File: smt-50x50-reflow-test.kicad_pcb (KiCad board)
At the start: 4 copper layers, 50 x 50 mm, 96 parts, among them J1 Conn_01x04_Pin, J2 Conn_01x02, J4 USB_C_Receptacle_USB2.0_14P, J8 Conn_01x04_Pin, J9 Conn_01x03_Pin, SW1 SW_Push, SW2 SW_Push, U1 ESP32-C6, U14 TMP117AIDRV, U15 BMP581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

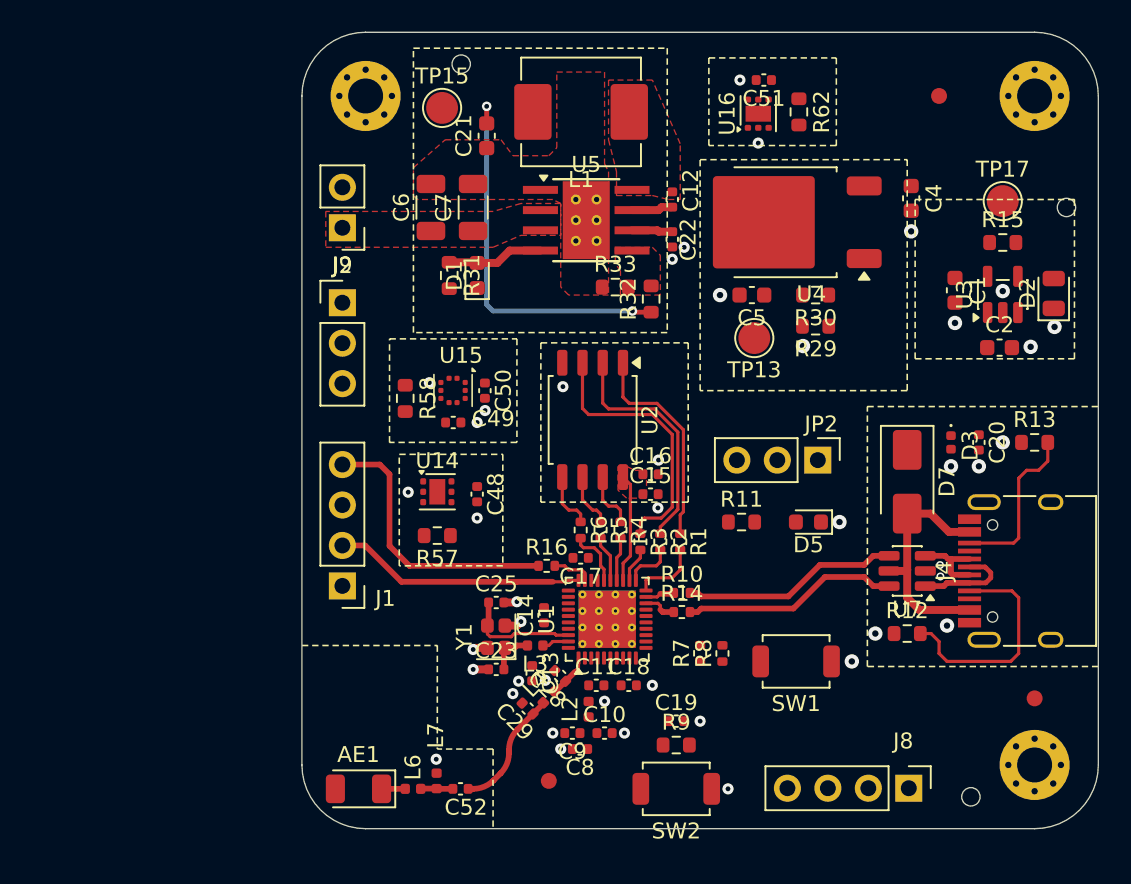
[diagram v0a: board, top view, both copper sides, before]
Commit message: pcb: add 3v3 routing
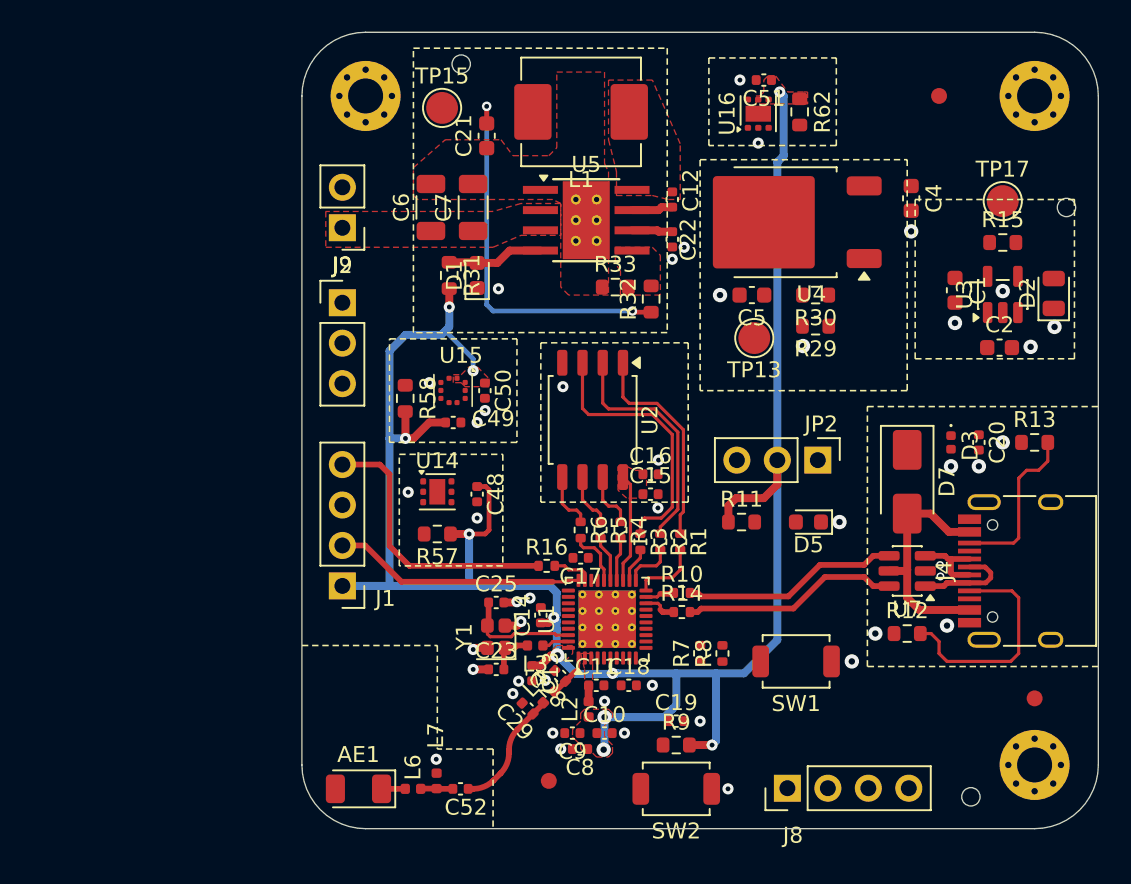
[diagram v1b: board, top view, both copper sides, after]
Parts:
- moved J8 7.62 mm to (165.5, 122.5), turned to 90 degrees
- moved C14 0.20 mm to (150.0, 111.6)
- moved R57 0.10 mm to (143.5, 106.5)
- moved R62 0.05 mm to (166.2, 80.0)
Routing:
- net +3V3: track 0.00 -> 131.3 mm, vias 0 -> 11
- net Net-(C11-Pad1): track 0.00 -> 1.02 mm
- net GND: vias 43 -> 45
- added copper zone on F.Cu, net +3V3
- added copper zone on F.Cu, net Net-(C11-Pad1)

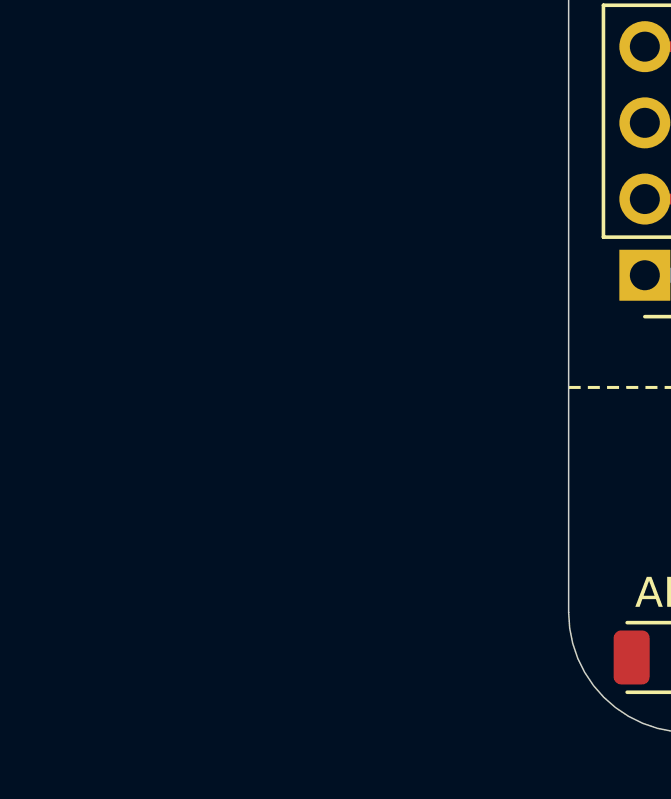
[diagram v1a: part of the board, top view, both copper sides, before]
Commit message: pcb: import smol area from schem
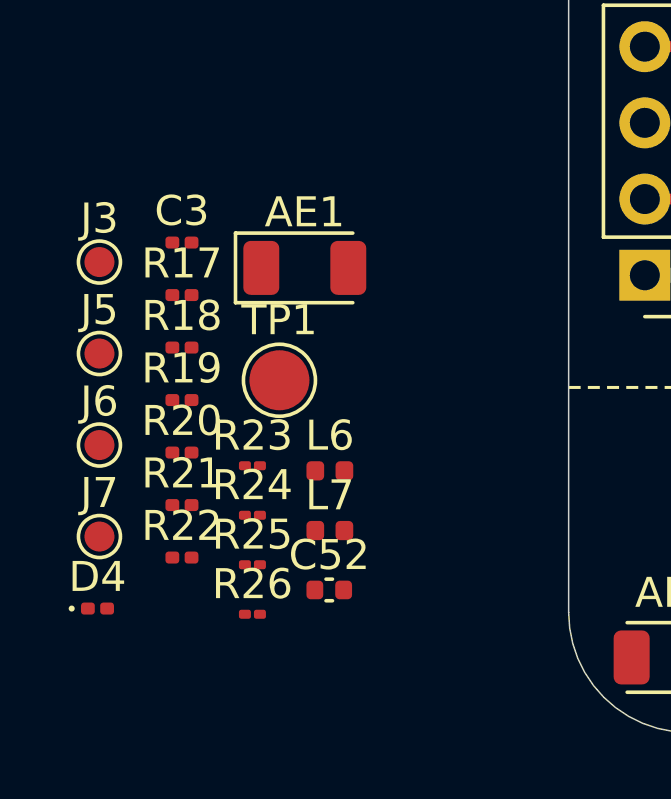
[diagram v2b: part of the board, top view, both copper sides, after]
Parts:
- added AE1: Antenna, RF_Antenna:Johanson_2450AT18x100, F.Cu at (126.2, 109.5)
- added C3: 2k2, Capacitor_SMD:C_0201_0603Metric, F.Cu at (122.1, 108.7)
- added C52: 1p, Capacitor_SMD:C_0402_1005Metric, F.Cu at (127.0, 120.2)
- added D4: ORANGE, LED_SMD:LED_0201_0603Metric, F.Cu at (119.3, 120.9)
- added J3: Conn_01x01, TestPoint:TestPoint_Pad_D1.0mm, F.Cu at (119.4, 109.3)
- added J5: Conn_01x01, TestPoint:TestPoint_Pad_D1.0mm, F.Cu at (119.4, 112.4)
- added J6: Conn_01x01, TestPoint:TestPoint_Pad_D1.0mm, F.Cu at (119.4, 115.4)
- added J7: Conn_01x01, TestPoint:TestPoint_Pad_D1.0mm, F.Cu at (119.4, 118.5)
- added L6: 3n9, Inductor_SMD:L_0402_1005Metric, F.Cu at (127.0, 116.3)
- added L7: 2n7, Inductor_SMD:L_0402_1005Metric, F.Cu at (127.0, 118.3)
- added R17: 5k1, Resistor_SMD:R_0201_0603Metric, F.Cu at (122.1, 110.4)
- added R18: 5k1, Resistor_SMD:R_0201_0603Metric, F.Cu at (122.1, 112.2)
- added R19: 10k, Resistor_SMD:R_0201_0603Metric, F.Cu at (122.1, 113.9)
- added R20: 24k, Resistor_SMD:R_0201_0603Metric, F.Cu at (122.1, 115.7)
- added R21: 70, Resistor_SMD:R_0201_0603Metric, F.Cu at (122.1, 117.4)
- added R22: 39k, Resistor_SMD:R_0201_0603Metric, F.Cu at (122.1, 119.2)
- added R23: 20k, Resistor_SMD:R_01005_0402Metric, F.Cu at (124.5, 116.1)
- added R24: 750, Resistor_SMD:R_01005_0402Metric, F.Cu at (124.5, 117.8)
- added R25: 1k33, Resistor_SMD:R_01005_0402Metric, F.Cu at (124.5, 119.4)
- added R26: 4k3, Resistor_SMD:R_01005_0402Metric, F.Cu at (124.5, 121.1)
- added TP1: TestPoint, TestPoint:TestPoint_Pad_D2.0mm, F.Cu at (125.4, 113.3)
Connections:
- U1 pad 31: unconnected-(U1-GPIO18/SDIO_CMD/FSPICS2-Pad31) -> Net-(U1-GPIO18/SDIO_CMD/FSPICS2)
- U1 pad 32: unconnected-(U1-GPIO19/SDIO_CLK/FSPICS3-Pad32) -> Net-(U1-GPIO19/SDIO_CLK/FSPICS3)
- U1 pad 34: unconnected-(U1-GPIO21/SDIO_DATA1/FSPICS5-Pad34) -> /BMP_INT1
- U1 pad 35: unconnected-(U1-GPIO22/SDIO_DATA2-Pad35) -> /TMP117_ALERT
- U1 pad 36: unconnected-(U1-GPIO23/SDIO_DATA3-Pad36) -> /TMP117_ALERT2
- U1 pad 6: /XTAL_32K_P -> unconnected-(U1-GPIO0/XTAL_32K_P/ADC1_CH0-Pad6)
- U1 pad 7: /XTAL_32K_N -> unconnected-(U1-GPIO1/XTAL_32K_N/ADC1_CH1-Pad7)

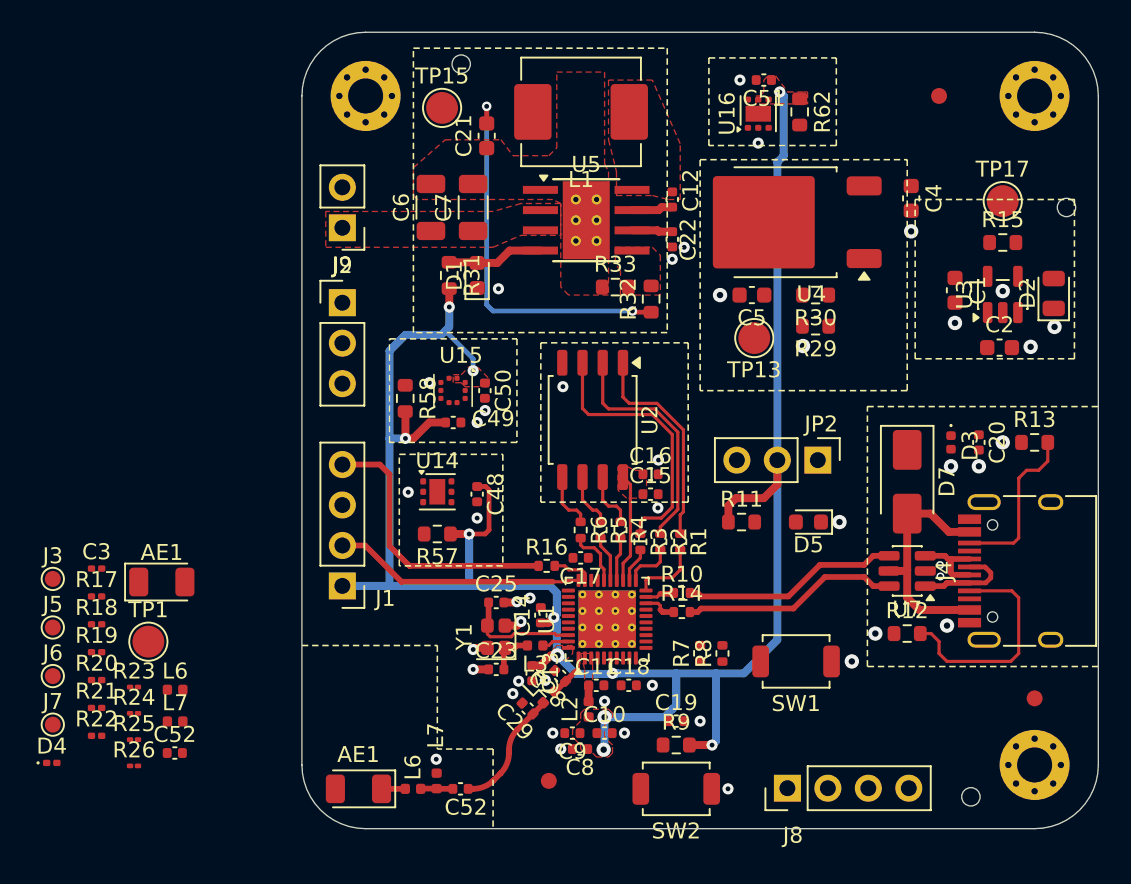
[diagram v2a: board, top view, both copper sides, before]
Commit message: pcb: add smol area layout
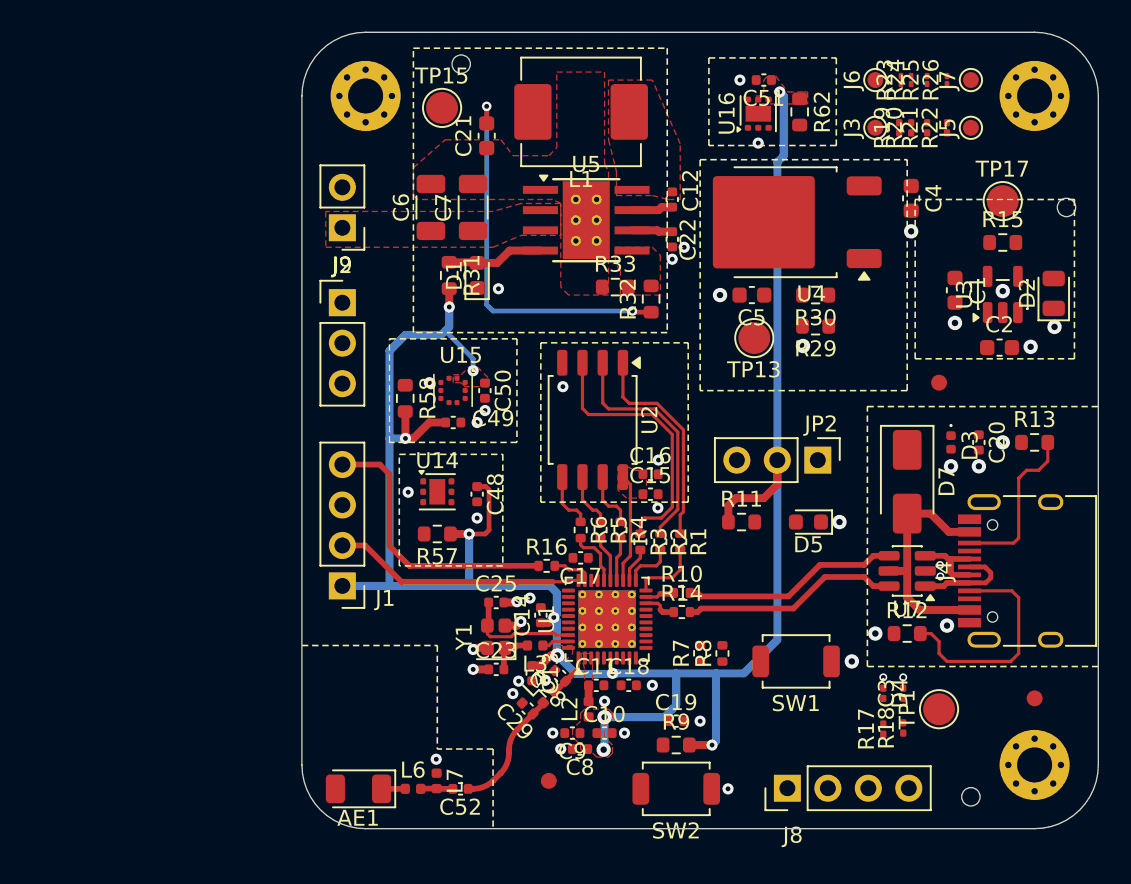
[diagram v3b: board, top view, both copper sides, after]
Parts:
- removed the AE1 at (138.6, 122.5)
- removed the C52 at (145.0, 122.5)
- removed the L6 at (142.0, 122.5)
- removed the L7 at (143.5, 122.0)
- moved J7 70.4 mm to (177.0, 78.0), turned to 90 degrees
- moved R26 66.8 mm to (175.5, 78.0), turned to 90 degrees
- moved R22 65.6 mm to (175.5, 81.0), turned to 90 degrees
- moved J5 65.6 mm to (177.0, 81.0), turned to 90 degrees
- moved R25 64.8 mm to (174.2, 78.0), turned to 90 degrees
- moved J6 63.8 mm to (171.0, 78.0), turned to 90 degrees
- moved R21 63.6 mm to (174.2, 81.0), turned to 90 degrees
- moved R24 62.9 mm to (173.2, 78.0), turned to 90 degrees
- moved R20 61.8 mm to (173.2, 81.0), turned to 90 degrees
- moved R23 61.4 mm to (172.6, 78.0), turned to 90 degrees
- moved R19 60.2 mm to (172.5, 81.0), turned to 90 degrees
- moved J3 58.9 mm to (171.0, 81.0), turned to 90 degrees
- moved D4 52.4 mm to (171.5, 116.5), turned to -90 degrees
- moved C3 51.2 mm to (172.8, 116.5), turned to 90 degrees
- moved R18 51.1 mm to (172.8, 118.7), turned to 90 degrees
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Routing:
- net GND: vias 45 -> 47

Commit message: pcb: add smol area routing
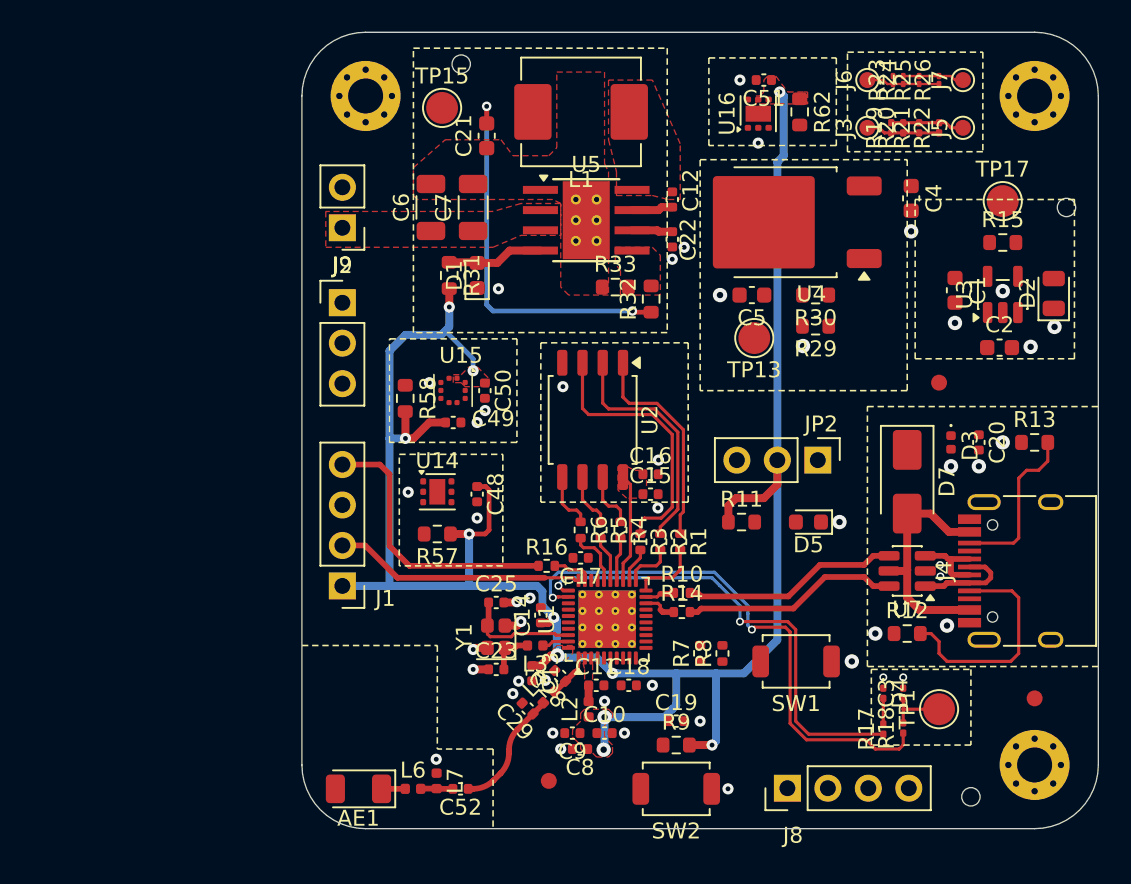
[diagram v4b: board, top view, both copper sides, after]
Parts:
- moved J3 0.50 mm to (170.5, 81.0)
- moved J5 0.50 mm to (176.5, 81.0)
- moved J6 0.50 mm to (170.5, 78.0)
- moved J7 0.50 mm to (176.5, 78.0)
- moved R19 0.50 mm to (172.0, 81.0)
- moved R20 0.50 mm to (172.8, 81.0)
- moved R21 0.50 mm to (173.8, 81.0)
- moved R22 0.50 mm to (175.0, 81.0)
- moved R23 0.50 mm to (172.1, 78.0)
- moved R24 0.50 mm to (172.8, 78.0)
- moved R25 0.50 mm to (173.8, 78.0)
- moved R26 0.50 mm to (175.0, 78.0)
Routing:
- net Net-(U1-GPIO19/SDIO_CLK/FSPICS3): track 0.00 -> 34.2 mm, vias 0 -> 2
- net Net-(U1-GPIO18/SDIO_CMD/FSPICS2): track 0.00 -> 29.4 mm, vias 0 -> 2
- net Net-(J5-Pin_1): track 0.00 -> 4.63 mm
- net Net-(J3-Pin_1): track 0.00 -> 4.63 mm
- net Net-(J6-Pin_1): track 0.00 -> 4.60 mm
- net Net-(J7-Pin_1): track 0.00 -> 4.49 mm
- net Net-(C3-Pad1): track 0.00 -> 3.79 mm
- net Net-(D4-A): track 0.00 -> 1.61 mm
- net +3V3: track 131.3 -> 130.4 mm

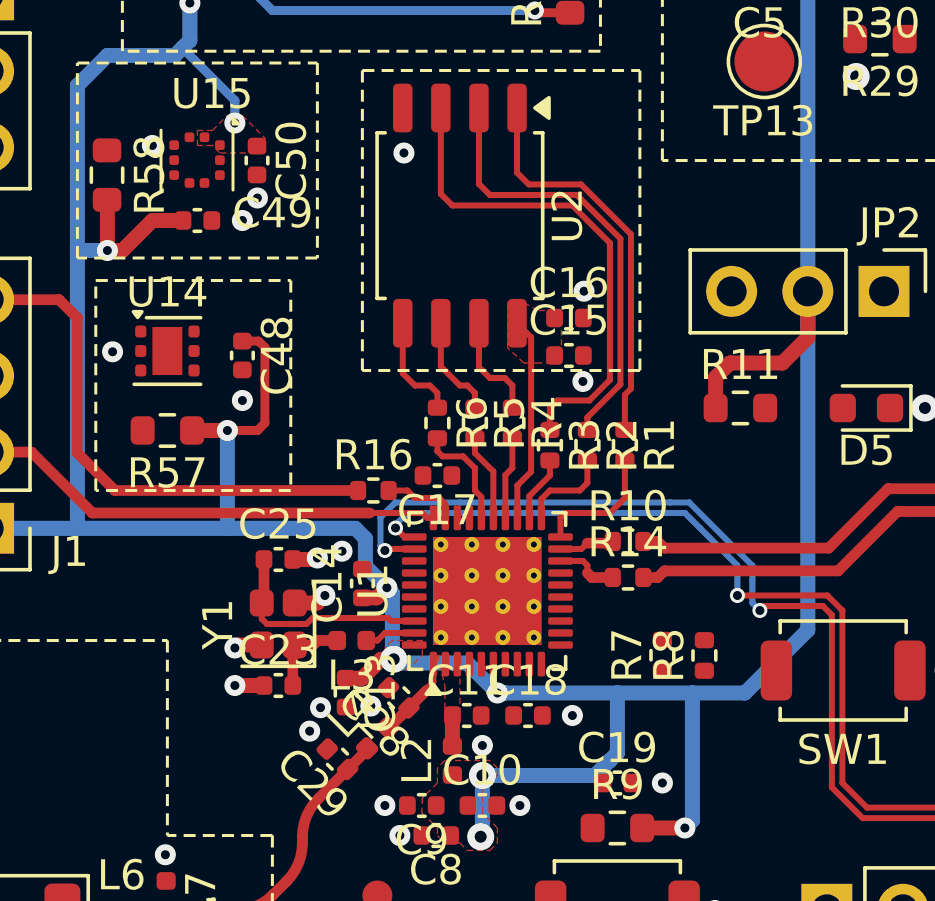
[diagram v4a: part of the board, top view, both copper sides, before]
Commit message: pcb: add missing 3v3 routing
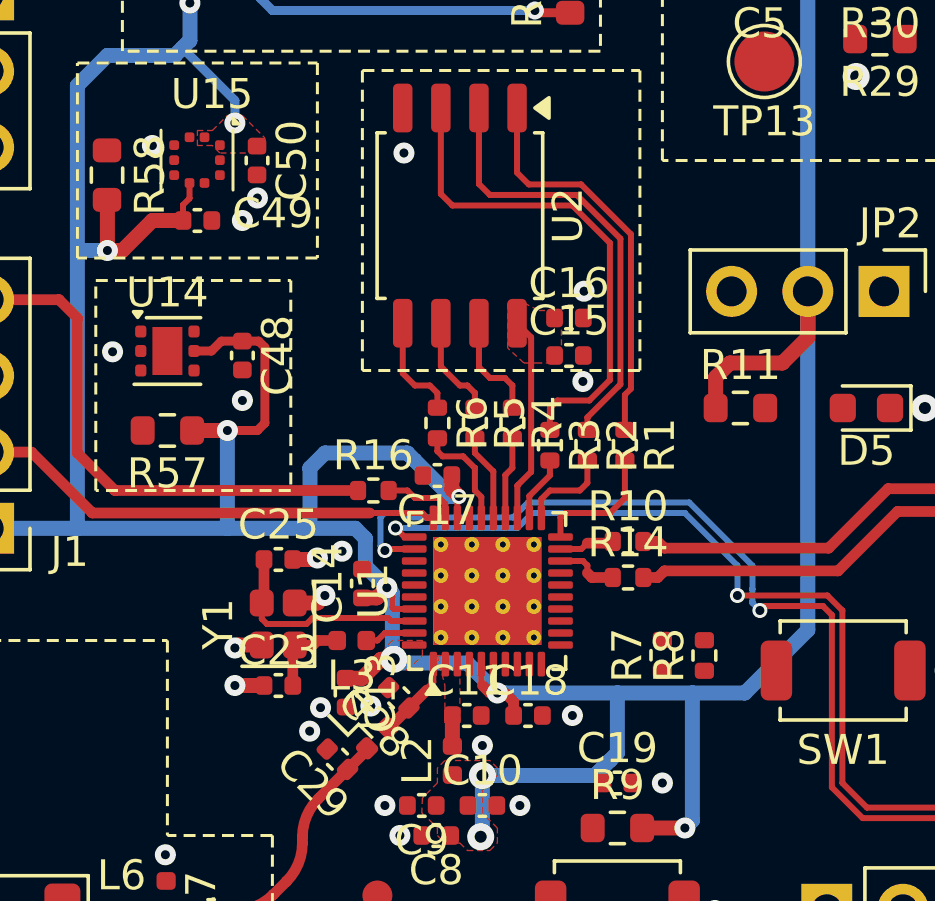
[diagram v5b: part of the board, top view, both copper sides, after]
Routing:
- net +3V3: track 130.4 -> 146.7 mm, vias 11 -> 12
